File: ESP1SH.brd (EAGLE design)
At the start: 53.3 x 53.3 mm, 28 parts, among them J1 Digital_0_7, J2 Analog, J3 Digital_8_13, J4 Power, J5 BT-TX, J6 Digital_0_7, J7 BT-RX, J8 ICSP, J9 ESP01, Q1 RJU003N03 N-MOSFET, Q2 RJU003N03 N-MOSFET

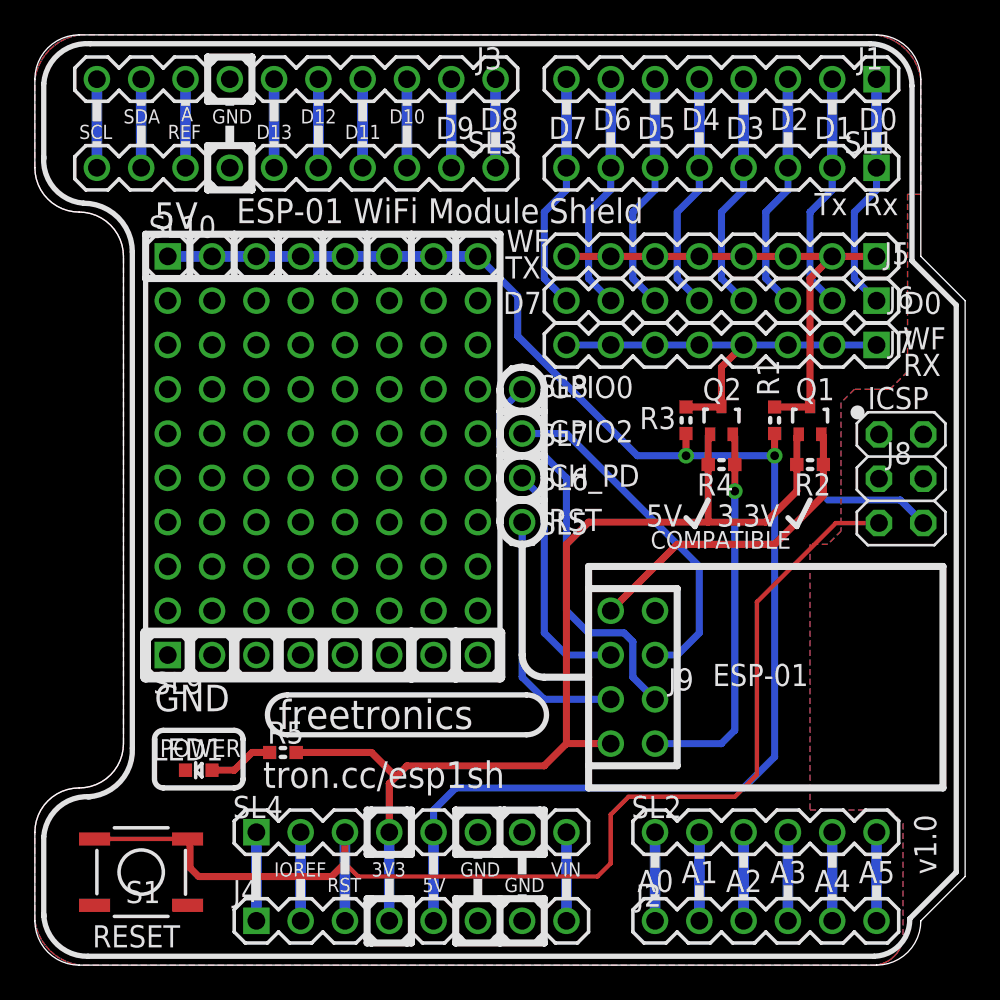
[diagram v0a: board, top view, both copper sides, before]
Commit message: Added onboard voltage regulator for v1.1 release
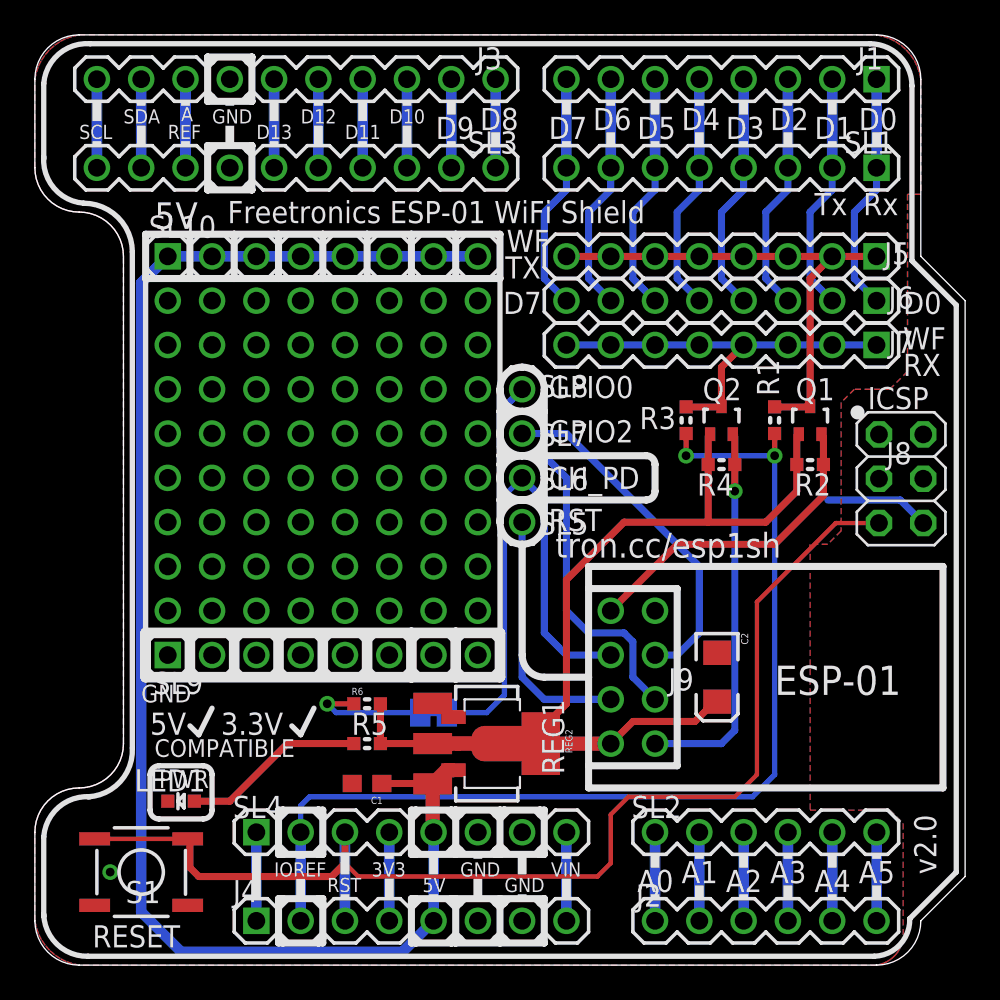
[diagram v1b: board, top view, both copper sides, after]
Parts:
- added C1: 1uF 0603, freetronics:0603
- added C2: 10uF 6.3V A TANT, freetronics:EIA3216
- added R6: 10K, freetronics-jon:0603
- added REG1: LD1117-SOT89, freetronics:SOT89
- added REG2: LD1117-SOT223, freetronics:SOT223
- added SJ1: ENABLE, freetronics-jon:SJC
- moved R5 4.85 mm to (19.1, 12.7)
- moved LED1 2.05 mm to (8.38, 9.40)
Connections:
- new net N$58: J4.4, SL4.4
- new net N$60: R6.1, SJ1.1
- net 3.3V: now also C2.A, R6.2, REG1.2, REG1.4, REG2.2, REG2.4; no longer J4.4, SL4.4
- net 5V: now also C1.1, REG1.3, REG2.3; no longer R1.2, R3.2
- net GND: now also C1.2, C2.C, REG1.1, REG2.1
- net IOREF: now also R1.2, R3.2
- net N$4: now also SJ1.2
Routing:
- net IOREF: track 5.08 -> 60.4 mm, vias 0 -> 2
- net N$4: track 13.8 -> 30.6 mm
- net N$60: track 0.00 -> 7.07 mm, vias 0 -> 1
- net N$14: track 3.72 -> 10.5 mm
- net N$58: track 0.00 -> 5.08 mm
- net 3.3V: track 62.1 -> 57.8 mm
- net 5V: track 87.9 -> 86.8 mm, vias 2 -> 0
- net GND: vias 0 -> 1
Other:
- board text added: "1 x 2K2 0603 5 x 10K 0603 1 x 1uF 0603 1 x 10uF 6.3V TANT 1 x BLUE LED 0603 2 x RJU003N03 1 x LD1117 1 x SMT TACT BUTTON"
- board text added: "CH_PD PULLUP"
- board text added: "CH_PD biased HIGH by default"
- board text added: "Freetronics ESP-01 WiFi Shield"
- board text added: "PWR"
- board text added: "v2.0"
- board text added: "www.freetronics.com"
- board text removed: "ESP-01 WiFi Module Shield"
- board text removed: "POWER"
- board text removed: "v1.0"

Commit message: Added REFLASH button connected to CH_PD
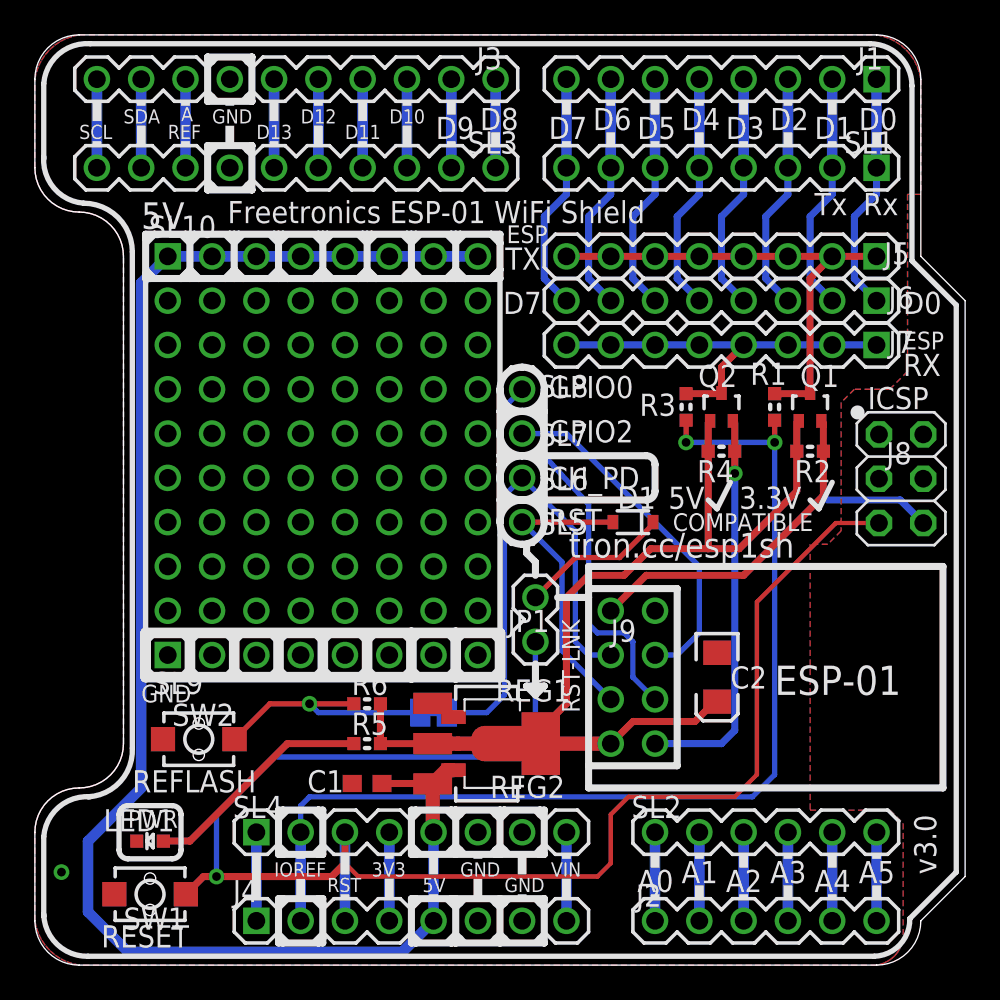
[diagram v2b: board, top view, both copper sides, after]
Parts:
- removed S1: RESET, freetronics-original:TACTILE_SWITCH_SMD
- added D1: 1N4148WS, freetronics-original:SOD-323
- added JP1: RST-LNK, freetronics-original:1X02
- added SW1: RESET, freetronics-master-v1:TACTILE_SWITCH_SMD_2PIN_TINY
- added SW2: REFLASH, freetronics-master-v1:TACTILE_SWITCH_SMD_2PIN_TINY
- moved LED1 2.90 mm to (6.60, 7.11)
- moved Q1 0.76 mm to (44.5, 32.0)
- moved Q2 0.76 mm to (39.4, 32.0)
- moved R1 0.76 mm to (42.4, 32.0)
- moved R2 0.76 mm to (44.5, 29.5)
- moved R3 0.76 mm to (37.3, 32.0)
- moved R4 0.76 mm to (39.4, 29.5)
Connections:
- new net N$61: D1.1, JP1.2
- net GND: now also SW1.2, SW2.2; no longer S1.1, S1.2
- net N$3: now also D1.2
- net N$60: now also SW2.1
- net RESET: now also JP1.1, SW1.1; no longer S1.3, S1.4
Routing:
- net RESET: track 70.1 -> 92.1 mm, vias 0 -> 1
- net N$61: track 0.00 -> 8.57 mm
- net N$60: track 7.07 -> 14.2 mm
- net 5V: track 86.8 -> 91.1 mm
- net N$3: track 14.5 -> 17.5 mm
- net N$14: track 10.5 -> 13.2 mm
- net 3.3V: track 57.8 -> 60.3 mm
- net TX: track 29.0 -> 28.2 mm
- net RX: track 23.9 -> 23.1 mm
- net N$45: track 21.9 -> 22.7 mm
- net N$44: track 18.5 -> 19.3 mm
- net IOREF: track 60.4 -> 61.2 mm
- net N$4: track 30.6 -> 29.8 mm
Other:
- board text added: "(c) 2015 Freetronics Pty Ltd Released under the TAPR Open Hardware License www.tapr.org/OHL"
- board text added: "1 x 2K2 0603 5 x 10K 0603 1 x 1uF 0603 1 x 10uF 6.3V TANT 1 x BLUE LED 0603 2 x RJU003N03 1 x LD1117 1 x 1N4148WS diode 2 x SMT TACT BUTTON"
- board text added: "CH_PD BIAS"
- board text added: "ESP"
- board text added: "REFLASH"
- board text added: "RST-LNK"
- board text added: "SW1"
- board text added: "SW2"
- board text added: "v3.0"
- board text removed: "(c) 2014 Freetronics Pty Ltd Released under the TAPR Open Hardware License www.tapr.org/OHL"
- board text removed: "1 x 2K2 0603 5 x 10K 0603 1 x 1uF 0603 1 x 10uF 6.3V TANT 1 x BLUE LED 0603 2 x RJU003N03 1 x LD1117 1 x SMT TACT BUTTON"
- board text removed: "CH_PD PULLUP"
- board text removed: "WF"
- board text removed: "v2.0"

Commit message: Changed REFLASH button from CH_PD to GPIO0
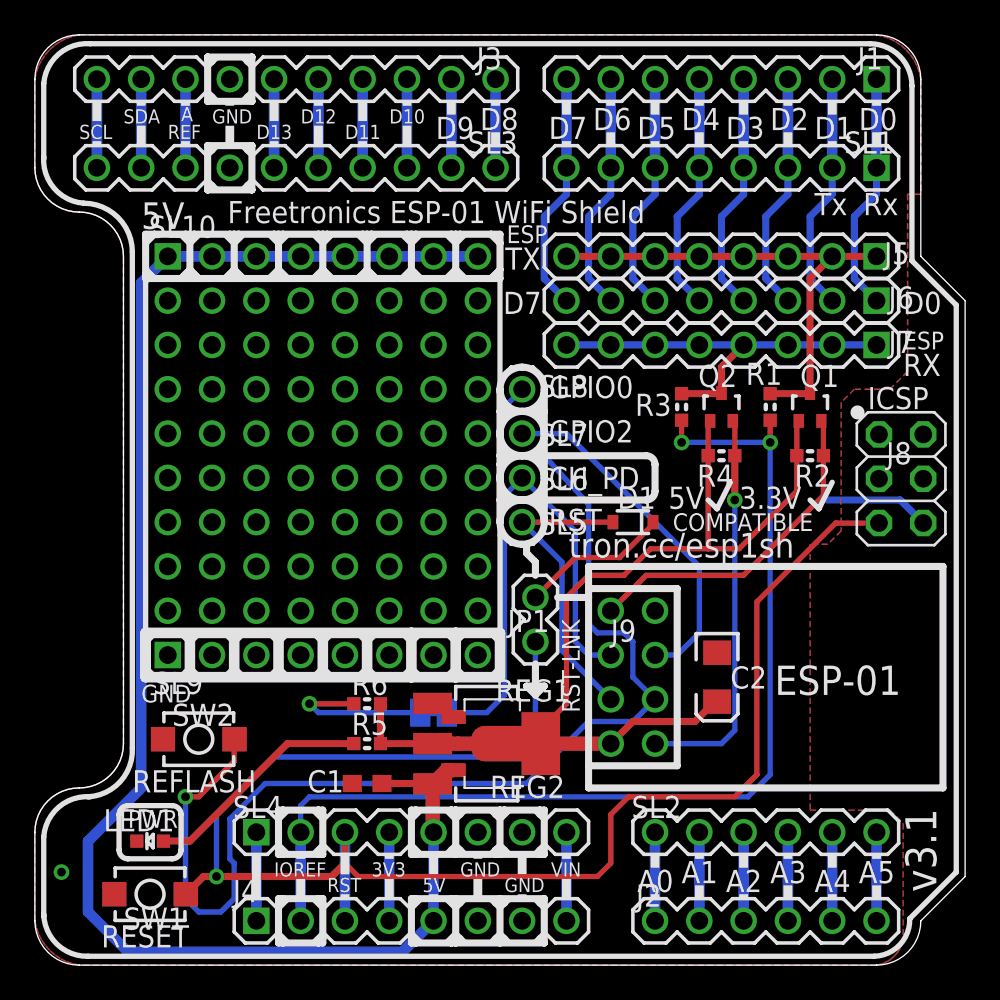
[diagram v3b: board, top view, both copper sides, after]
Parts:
- SW1, SW2: device freetronics-master-v1:TACTILE_SWITCH_SMD_2PIN_TINY -> freetronics-jon:TACTILE_SWITCH_SMD_2PIN_TINY
- moved R1 0.25 mm to (42.2, 32.0)
- moved R2 0.25 mm to (44.5, 29.2)
- moved R3 0.25 mm to (37.1, 32.0)
- moved R4 0.25 mm to (39.4, 29.2)
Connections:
- net N$1: now also SW2.1
- net N$60: no longer SW2.1
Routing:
- net N$1: track 24.0 -> 70.1 mm, vias 0 -> 1
- net N$60: track 14.2 -> 9.10 mm
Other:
- board text added: "CH_PD biased HIGH by default GPIO0 pulled LOW by REFLASH"
- board text added: "v3.1"
- board text removed: "CH_PD biased HIGH by default"
- board text removed: "v3.0"
